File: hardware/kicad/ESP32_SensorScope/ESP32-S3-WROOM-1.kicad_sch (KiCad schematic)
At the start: 1 part, among them U2 ESP32-S3-WROOM-1

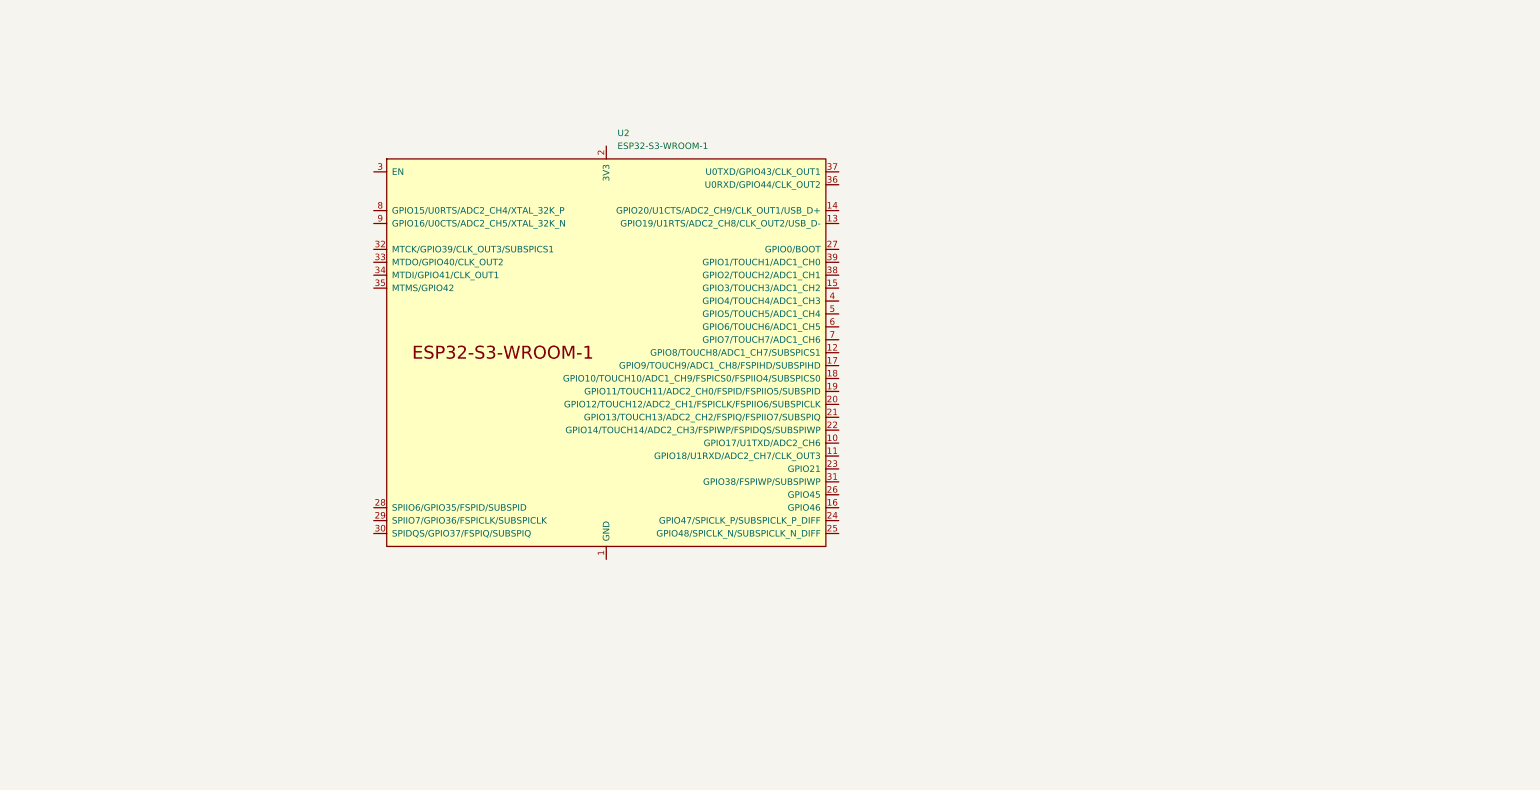
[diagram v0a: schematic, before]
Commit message: Added serial interfases
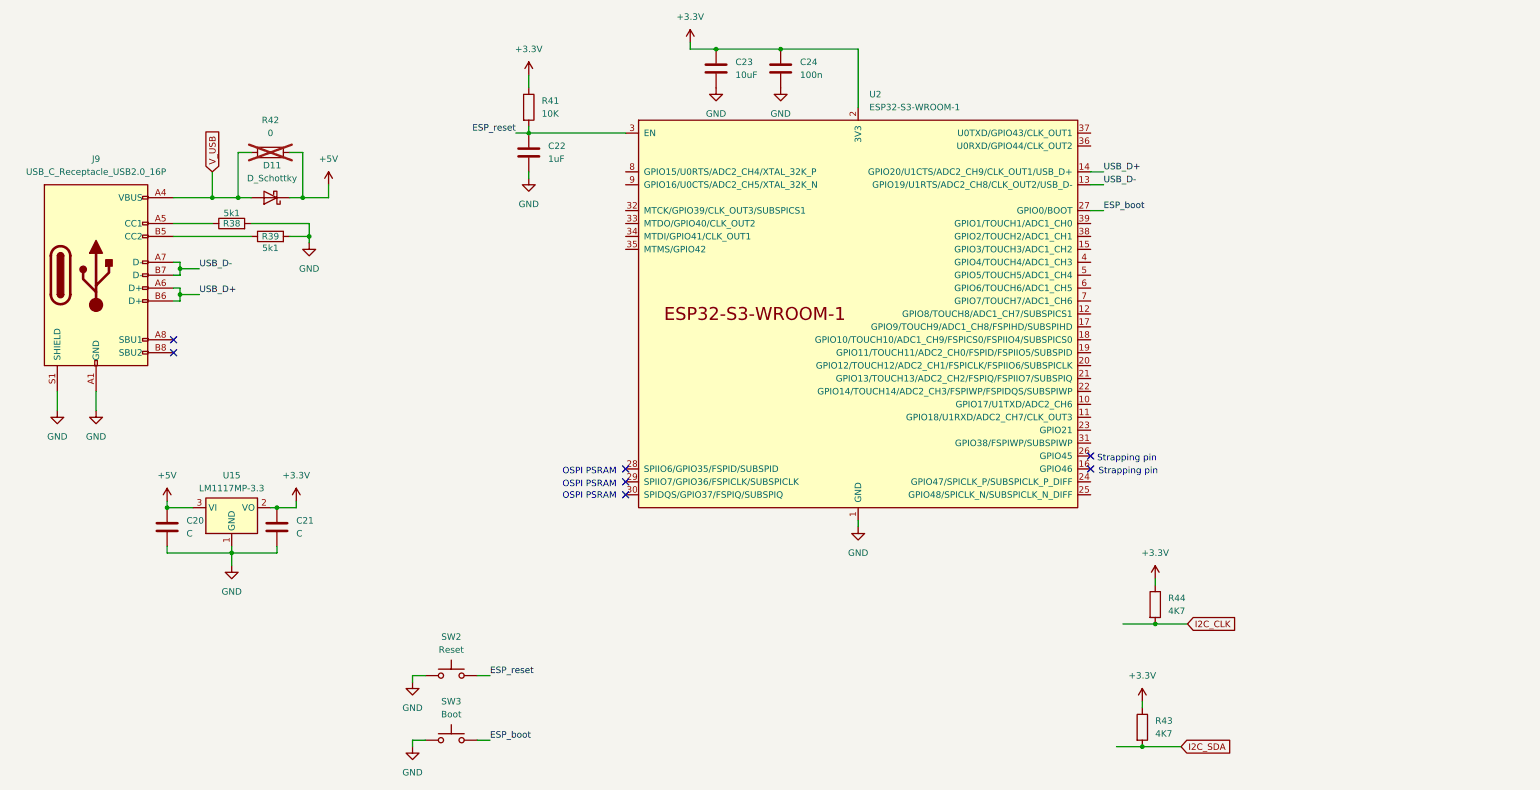
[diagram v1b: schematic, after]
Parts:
- added C20, C21: C, symbol Device:C
- added C22: 1uF, symbol Device:C
- added C23: 10uF, symbol Device:C
- added C24: 100n, symbol Device:C
- added D11: D_Schottky, symbol Device:D_Schottky
- added J9: USB_C_Receptacle_USB2.0_16P, symbol Connector:USB_C_Receptacle_USB2.0_16P
- added R38, R39: 5k1, symbol Device:R
- added R41: 10K, symbol Device:R
- added R42: 0, symbol Device:R
- added R43, R44: 4K7, symbol Device:R
- added SW2: Reset, symbol Switch:SW_Push
- added SW3: Boot, symbol Switch:SW_Push
- added U15: LM1117MP-3.3, Package_TO_SOT_SMD:SOT-223-3_TabPin2, symbol Regulator_Linear:LM1117MP-3.3
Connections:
- net GND: now reaches U2.1 (GND), U2.40 (GND), U2.41 (GND)
- net GND: now also C20.2, C21.2, C22.2, C23.2, C24.2, J9.A1 (GND), J9.A12 (GND), J9.B1 (GND), J9.B12 (GND), J9.S1 (SHIELD), R38.2, R39.2, SW2.1, SW3.1, U15.1 (GND)
- net USB_D-: now reaches U2.13 (GPIO19/U1RTS/ADC2_CH8/CLK_OUT2/USB_D-)
- net USB_D-: now also J9.A7 (D-), J9.B7 (D-)
- net USB_D+: now reaches U2.14 (GPIO20/U1CTS/ADC2_CH9/CLK_OUT1/USB_D+)
- net USB_D+: now also J9.A6 (D+), J9.B6 (D+)
- net +3.3V: now reaches U2.2 (3V3)
- net +3.3V: now also C21.1, C23.1, C24.1, R41.1, R43.1, R44.1, U15.2 (VO)
- net ESP_boot: now reaches U2.27 (GPIO0/BOOT)
- net ESP_boot: now also SW3.2
- net ESP_reset: now reaches U2.3 (EN)
- net ESP_reset: now also C22.1, R41.2, SW2.2
- new net: J9.A5 (CC1), R38.1
- new net: J9.B5 (CC2), R39.1
- new net +5V: C20.1, D11.1 (K), R42.2, U15.3 (VI)
- new net I2C_CLK: R44.2
- new net I2C_SDA: R43.2
- new net V_USB: D11.2 (A), J9.A4 (VBUS), J9.A9 (VBUS), J9.B4 (VBUS), J9.B9 (VBUS), R42.1
- no-connect marks 0 -> 7
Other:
- note added: "OSPI PSRAM"
- note added: "Strapping pin"
- moved on the sheet: U2

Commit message: Adde LCD Part
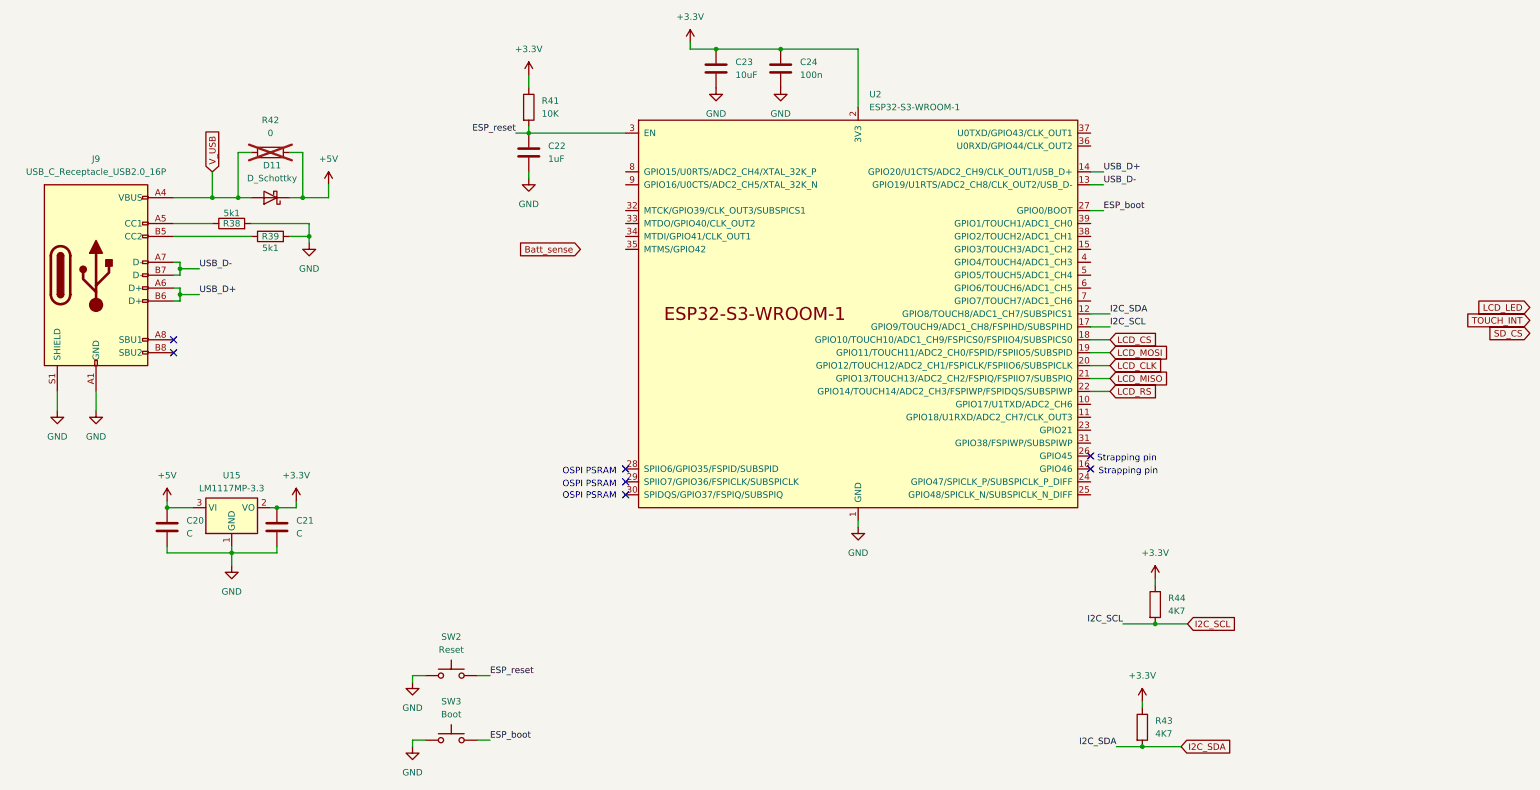
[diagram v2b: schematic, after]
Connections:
- net I2C_CLK is gone; now on net I2C_SCL: R44.2
- net I2C_SDA: now also U2.12 (GPIO8/TOUCH8/ADC1_CH7/SUBSPICS1)
- net I2C_SCL: now reaches U2.17 (GPIO9/TOUCH9/ADC1_CH8/FSPIHD/SUBSPIHD)
- net LCD_CS: now reaches U2.18 (GPIO10/TOUCH10/ADC1_CH9/FSPICS0/FSPIIO4/SUBSPICS0)
- net LCD_MOSI: now reaches U2.19 (GPIO11/TOUCH11/ADC2_CH0/FSPID/FSPIIO5/SUBSPID)
- net LCD_CLK: now reaches U2.20 (GPIO12/TOUCH12/ADC2_CH1/FSPICLK/FSPIIO6/SUBSPICLK)
- net LCD_MISO: now reaches U2.21 (GPIO13/TOUCH13/ADC2_CH2/FSPIQ/FSPIIO7/SUBSPIQ)
- net LCD_RS: now reaches U2.22 (GPIO14/TOUCH14/ADC2_CH3/FSPIWP/FSPIDQS/SUBSPIWP)

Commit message: something probobly
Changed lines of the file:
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@@
 		)
 	)
-	(global_label "Batt_sense"
+	(global_label "Ch2_ADC"
 		(shape input)
-		(at 137.16 59.69 180)
+		(at 132.08 71.12 180)
 		(fields_autoplaced yes)
 		(effects
@@
 		)
 		(property "Intersheetrefs" "${INTERSHEET_REFS}"
-			(at 123.9544 59.69 0)
+			(at 120.8701 71.12 0)
+			(effects
+				(font
+					(size 1.27 1.27)
+				)
+				(justify right)
+				(hide yes)
+			)
+		)
+	)
+	(global_label "Batt_ADC"
+		(shape input)
+		(at 132.08 63.5 180)
+		(fields_autoplaced yes)
+		(effects
+			(font
+				(size 1.27 1.27)
+			)
+			(justify right)
+		)
+		(property "Intersheetrefs" "${INTERSHEET_REFS}"
+			(at 120.6282 63.5 0)
 			(effects
 				(font
@@
 				)
 				(justify left)
+				(hide yes)
+			)
+		)
+	)
+	(global_label "mA_ADC"
+		(shape input)
+		(at 132.08 66.04 180)
+		(fields_autoplaced yes)
+		(effects
+			(font
+				(size 1.27 1.27)
+			)
+			(justify right)
+		)
+		(property "Intersheetrefs" "${INTERSHEET_REFS}"
+			(at 121.7167 66.04 0)
+			(effects
+				(font
+					(size 1.27 1.27)
+				)
+				(justify right)
 				(hide yes)
 			)
@@
 			(effects
 				(font
+					(size 1.27 1.27)
+				)
+				(justify right)
+				(hide yes)
+			)
+		)
+	)
+	(global_label "Ch1_ADC"
+		(shape input)
+		(at 132.08 68.58 180)
+		(fields_autoplaced yes)
+		(effects
+			(font
+				(size 1.27 1.27)
+			)
+			(justify right)
+		)
+		(property "Intersheetrefs" "${INTERSHEET_REFS}"
+			(at 120.8701 68.58 0)
+			(effects
+				(font

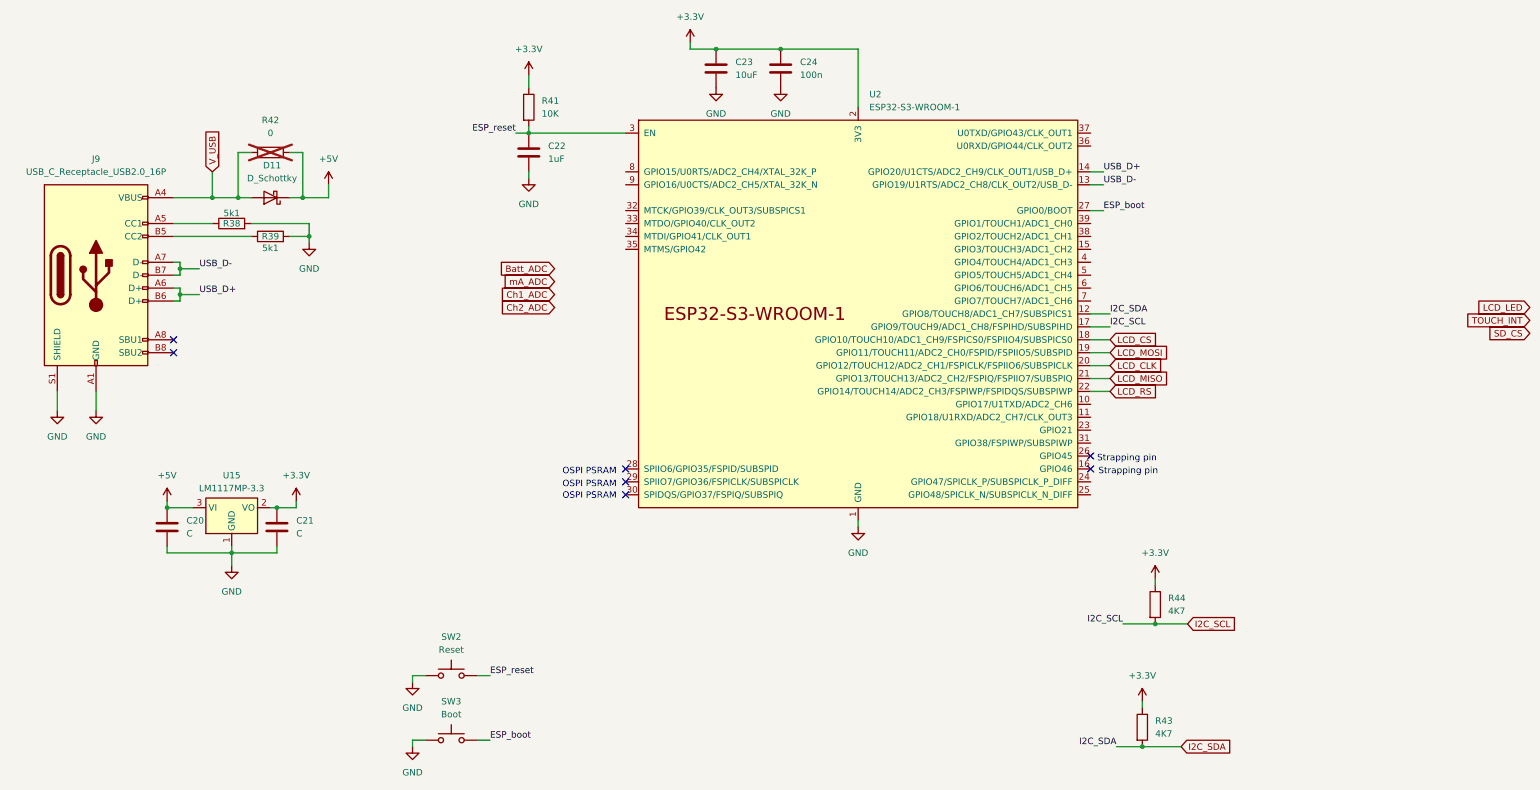
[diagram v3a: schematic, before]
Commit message: som updates on the schematics
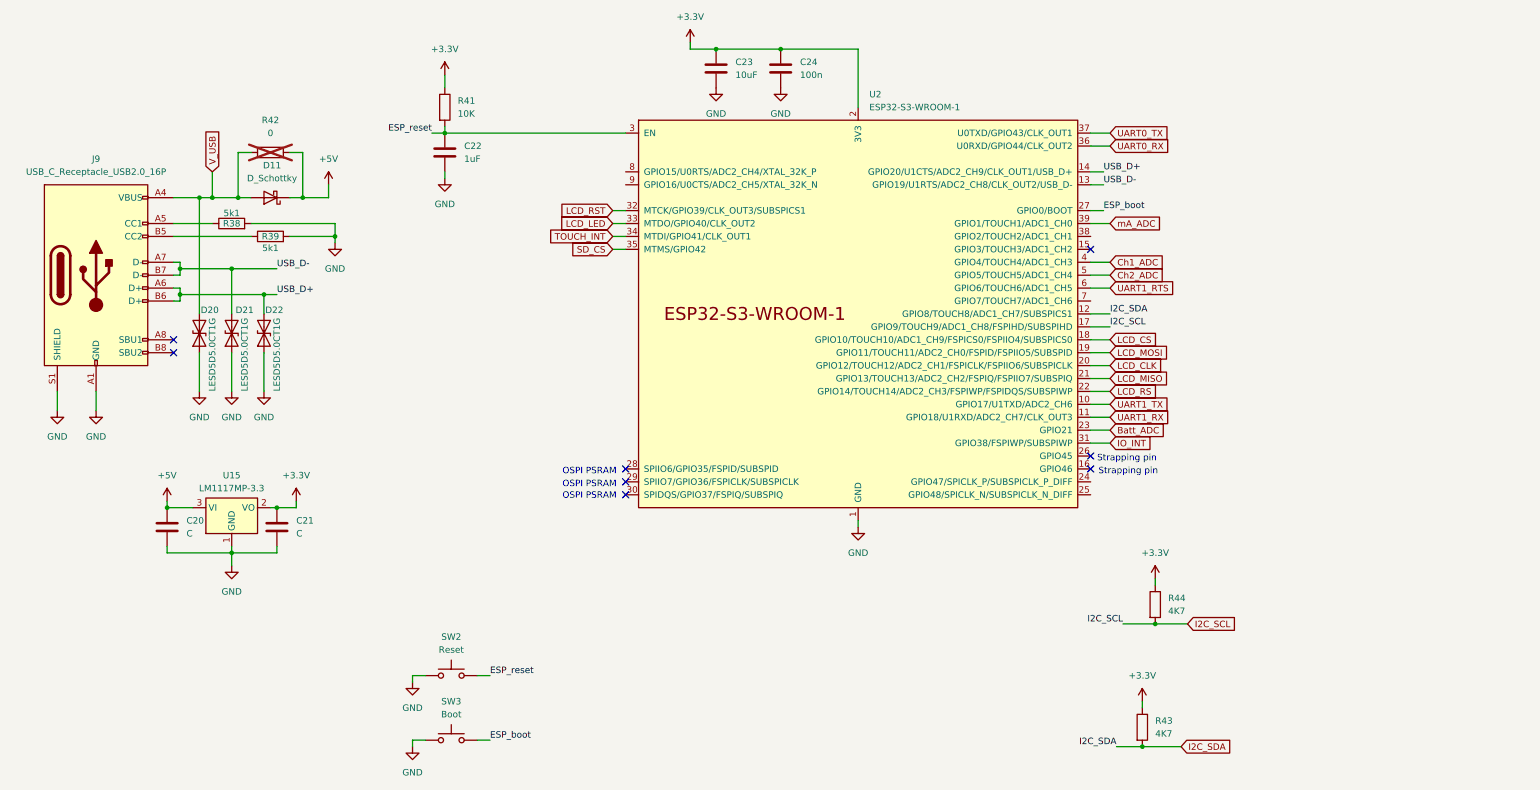
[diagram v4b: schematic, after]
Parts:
- added D20, D21, D22: LESD5D5.0CT1G, Diode_SMD:D_SOD-523, symbol Device:D_TVS
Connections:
- net Batt_ADC: now also U2.23 (GPIO21)
- net Ch1_ADC: now also U2.4 (GPIO4/TOUCH4/ADC1_CH3)
- net Ch2_ADC: now also U2.5 (GPIO5/TOUCH5/ADC1_CH4)
- net GND: now also D20.1 (A1), D21.1 (A1), D22.1 (A1)
- net LCD_LED: now also U2.33 (MTDO/GPIO40/CLK_OUT2)
- net SD_CS: now also U2.35 (MTMS/GPIO42)
- net TOUCH_INT: now also U2.34 (MTDI/GPIO41/CLK_OUT1)
- net USB_D+: now also D22.2 (A2)
- net USB_D-: now also D21.2 (A2)
- net V_USB: now also D20.2 (A2)
- net mA_ADC: now also U2.39 (GPIO1/TOUCH1/ADC1_CH0)
- net UART1_TX: now reaches U2.10 (GPIO17/U1TXD/ADC2_CH6)
- net UART1_RX: now reaches U2.11 (GPIO18/U1RXD/ADC2_CH7/CLK_OUT3)
- net IO_INT: now reaches U2.31 (GPIO38/FSPIWP/SUBSPIWP)
- net LCD_RST: now reaches U2.32 (MTCK/GPIO39/CLK_OUT3/SUBSPICS1)
- net UART0_RX: now reaches U2.36 (U0RXD/GPIO44/CLK_OUT2)
- net UART0_TX: now reaches U2.37 (U0TXD/GPIO43/CLK_OUT1)
- net UART1_RTS: now reaches U2.6 (GPIO6/TOUCH6/ADC1_CH5)
- no-connect marks 7 -> 8
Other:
- moved on the sheet: C22, R41

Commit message: updatet schematic
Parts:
- removed D20, D21, D22: LESD5D5.0CT1G, Diode_SMD:D_SOD-523, symbol Device:D_TVS
- removed U15: LM1117MP-3.3, Package_TO_SOT_SMD:SOT-223-3_TabPin2, symbol Regulator_Linear:LM1117MP-3.3
- added TP1, TP2: TestPoint, symbol Connector:TestPoint
- added U16: TLV76133DCY, Package_TO_SOT_SMD:SOT-223-3_TabPin2, symbol Regulator_Linear:TLV76133DCY
- added U27: USBLC6-2SC6, Package_TO_SOT_SMD:SOT-23-6, symbol Power_Protection:USBLC6-2SC6
- C20: value C -> 1uF
- C21: value C -> 2.2uF
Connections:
- net +3.3V: now also U16.2 (VO)
- net +5V: now also U16.3 (VI), U27.5 (VBUS)
- net GND: now also U16.1 (GND), U27.2 (GND)
- net USB_D+: now also U27.4 (I/O2); no longer J9.A6 (D+), J9.B6 (D+)
- net USB_D-: now also U27.6 (I/O1); no longer J9.A7 (D-), J9.B7 (D-)
- net at U2.24 (GPIO47/SPICLK_P/SUBSPICLK_P_DIFF): now also TP1.1
- net at U2.25 (GPIO48/SPICLK_N/SUBSPICLK_N_DIFF): now also TP2.1
- new net: J9.A7 (D-), J9.B7 (D-), U27.1 (I/O1)
- new net: J9.A6 (D+), J9.B6 (D+), U27.3 (I/O2)
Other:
- note added: "LDO max current 500mA / 0.85W"
- note added: "Strapping pins"
- note removed: "Strapping pin"
- moved on the sheet: C20, D11, R38, R39
